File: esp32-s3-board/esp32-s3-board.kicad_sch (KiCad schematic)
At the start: 23 parts, among them J1 5077CR-16SMC2-BK-TR, Q1 UMH3N, U1 USBLC6-2P6, U2 LDL1117S33R, U3 CP2102N-Axx-xQFN28, U4 ESP32-S3-WROOM-1

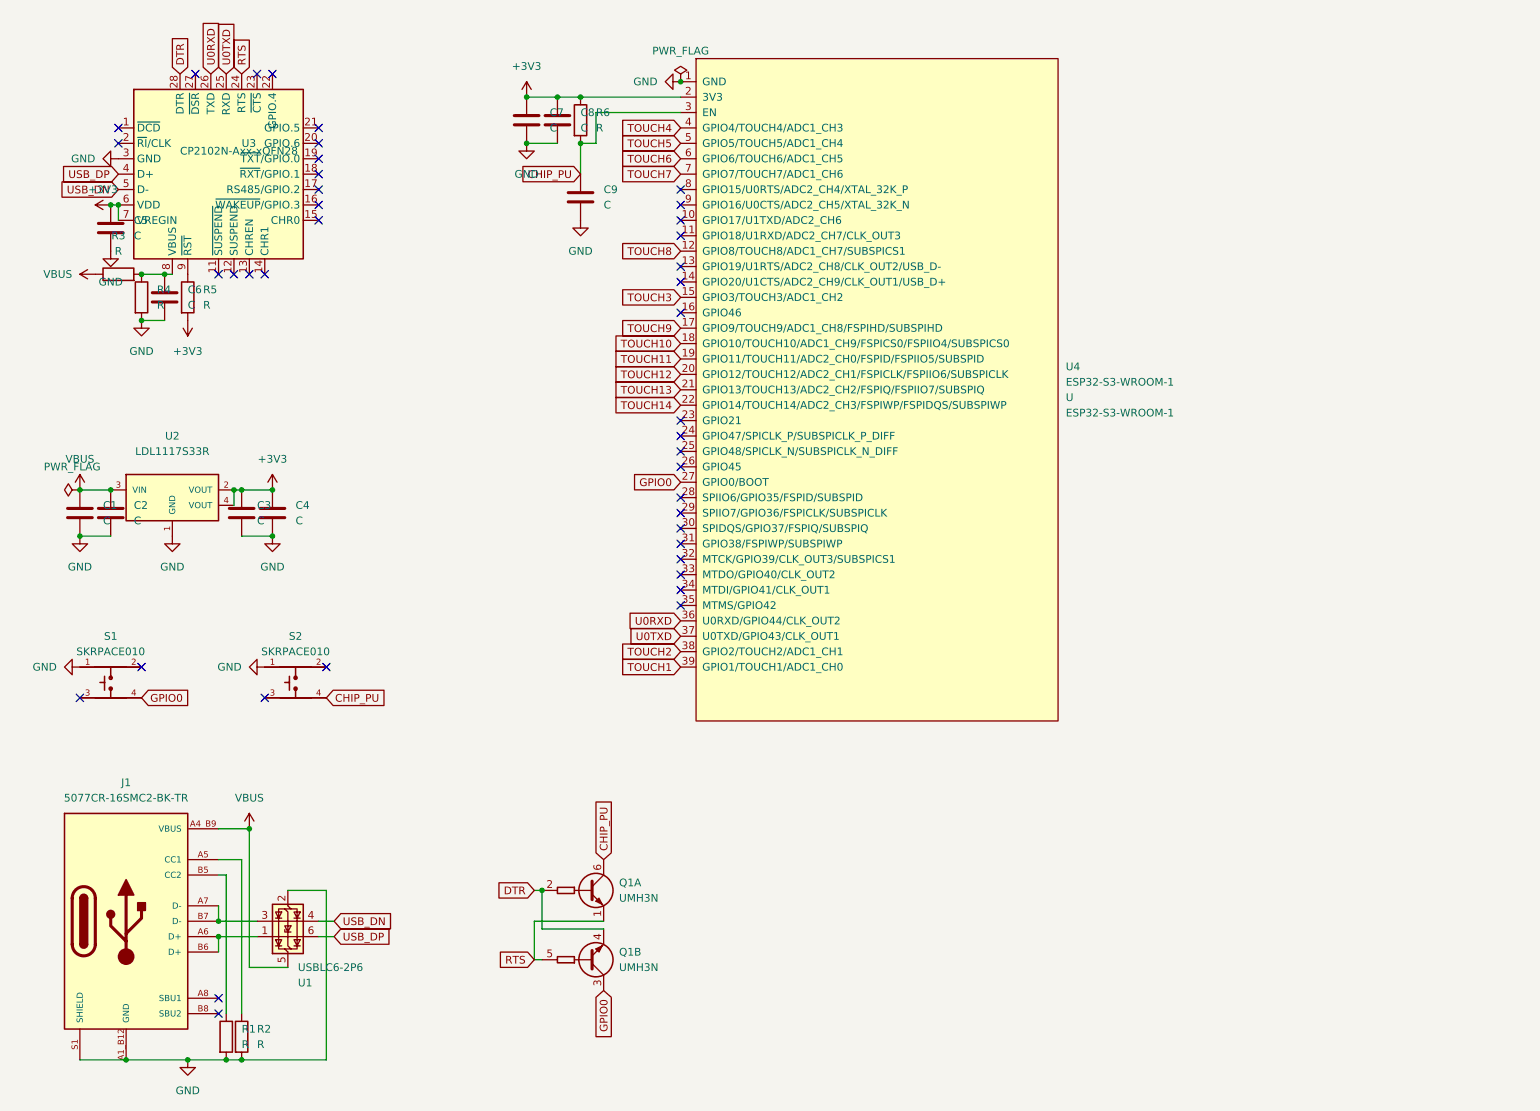
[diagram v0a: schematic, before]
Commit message: Add symbols and footprints libraries to esp32-s3-board
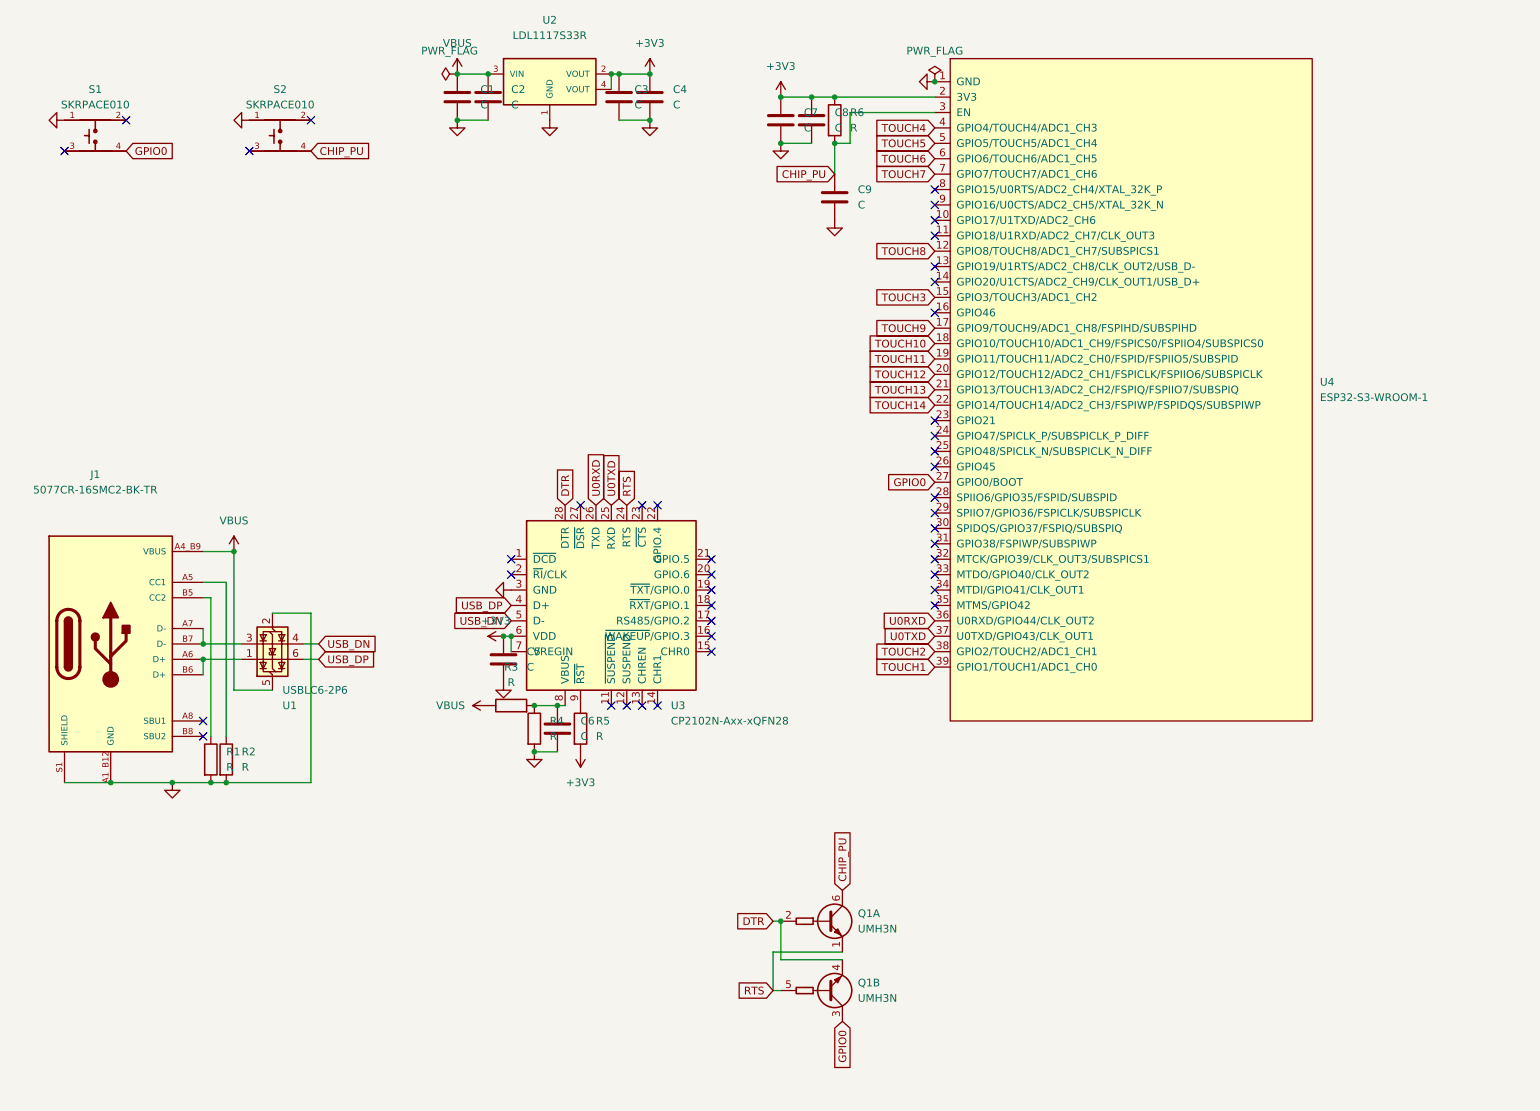
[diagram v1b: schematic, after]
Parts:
- removed U3: CP2102N-Axx-xQFN28, Package_DFN_QFN:QFN-28-1EP_5x5mm_P0.5mm_EP3.35x3.35mm, symbol Interface_USB:CP2102N-Axx-xQFN28
- removed U4: ESP32-S3-WROOM-1, RF_Module:ESP32-S3-WROOM-1, symbol Espressif:ESP32-S3-WROOM-1
- added U3: CP2102N-Axx-xQFN28, Package_DFN_QFN:QFN-28-1EP_5x5mm_P0.5mm_EP3.35x3.35mm, symbol CP2102N-Axx-xQFN28:CP2102N-Axx-xQFN28
- added U4: ESP32-S3-WROOM-1, RF_Module:ESP32-S3-WROOM-1, symbol ESP32-S3-WROOM-1:ESP32-S3-WROOM-1
- J1: footprint 5077CR-16SMC2-BK-TR:NELTRON_5077CR-16SMC2-BK-TR -> 5077CR-16SMC2-BK-TR:5077CR-16SMC2-BK-TR
- S1, S2: footprint SKRPACE010:SW_SKRPACE010 -> SKRPACE010:SKRPACE010
- U2: footprint LDL1117S33R:SOT230P700X180-4N -> LDL1117S33R:LDL1117S33R
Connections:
- net +3V3: now also U3.6 (VDD), U3.7 (VREGIN), U4.2 (3V3)
- net CHIP_PU: now also U4.3 (EN)
- net DTR: now also U3.28 (DTR)
- net GPIO0: now also U4.27 (GPIO0/BOOT)
- net RTS: now also U3.24 (RTS)
- net TOUCH1: now also U4.39 (GPIO1/TOUCH1/ADC1_CH0)
- net TOUCH10: now also U4.18 (GPIO10/TOUCH10/ADC1_CH9/FSPICS0/FSPIIO4/SUBSPICS0)
- net TOUCH11: now also U4.19 (GPIO11/TOUCH11/ADC2_CH0/FSPID/FSPIIO5/SUBSPID)
- net TOUCH12: now also U4.20 (GPIO12/TOUCH12/ADC2_CH1/FSPICLK/FSPIIO6/SUBSPICLK)
- net TOUCH13: now also U4.21 (GPIO13/TOUCH13/ADC2_CH2/FSPIQ/FSPIIO7/SUBSPIQ)
- net TOUCH14: now also U4.22 (GPIO14/TOUCH14/ADC2_CH3/FSPIWP/FSPIDQS/SUBSPIWP)
- net TOUCH2: now also U4.38 (GPIO2/TOUCH2/ADC1_CH1)
- net TOUCH3: now also U4.15 (GPIO3/TOUCH3/ADC1_CH2)
- net TOUCH4: now also U4.4 (GPIO4/TOUCH4/ADC1_CH3)
- net TOUCH5: now also U4.5 (GPIO5/TOUCH5/ADC1_CH4)
- net TOUCH6: now also U4.6 (GPIO6/TOUCH6/ADC1_CH5)
- net TOUCH7: now also U4.7 (GPIO7/TOUCH7/ADC1_CH6)
- net TOUCH8: now also U4.12 (GPIO8/TOUCH8/ADC1_CH7/SUBSPICS1)
- net TOUCH9: now also U4.17 (GPIO9/TOUCH9/ADC1_CH8/FSPIHD/SUBSPIHD)
- net U0RXD: now also U3.26 (TXD), U4.36 (U0RXD/GPIO44/CLK_OUT2)
- net U0TXD: now also U3.25 (RXD), U4.37 (U0TXD/GPIO43/CLK_OUT1)
- net USB_DN: now also U3.5 (D-)
- net USB_DP: now also U3.4 (D+)
- net at C6.2, R3.2, R4.1: now also U3.8 (VBUS)
- net at R5.1: now also U3.9 (~{RST})
- net GND renamed Earth
- net Earth: now also U3.29 (GND), U3.3 (GND), U4.1 (GND), U4.40 (GND), U4.41 (GND)

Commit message: Complete esp32-s3-board
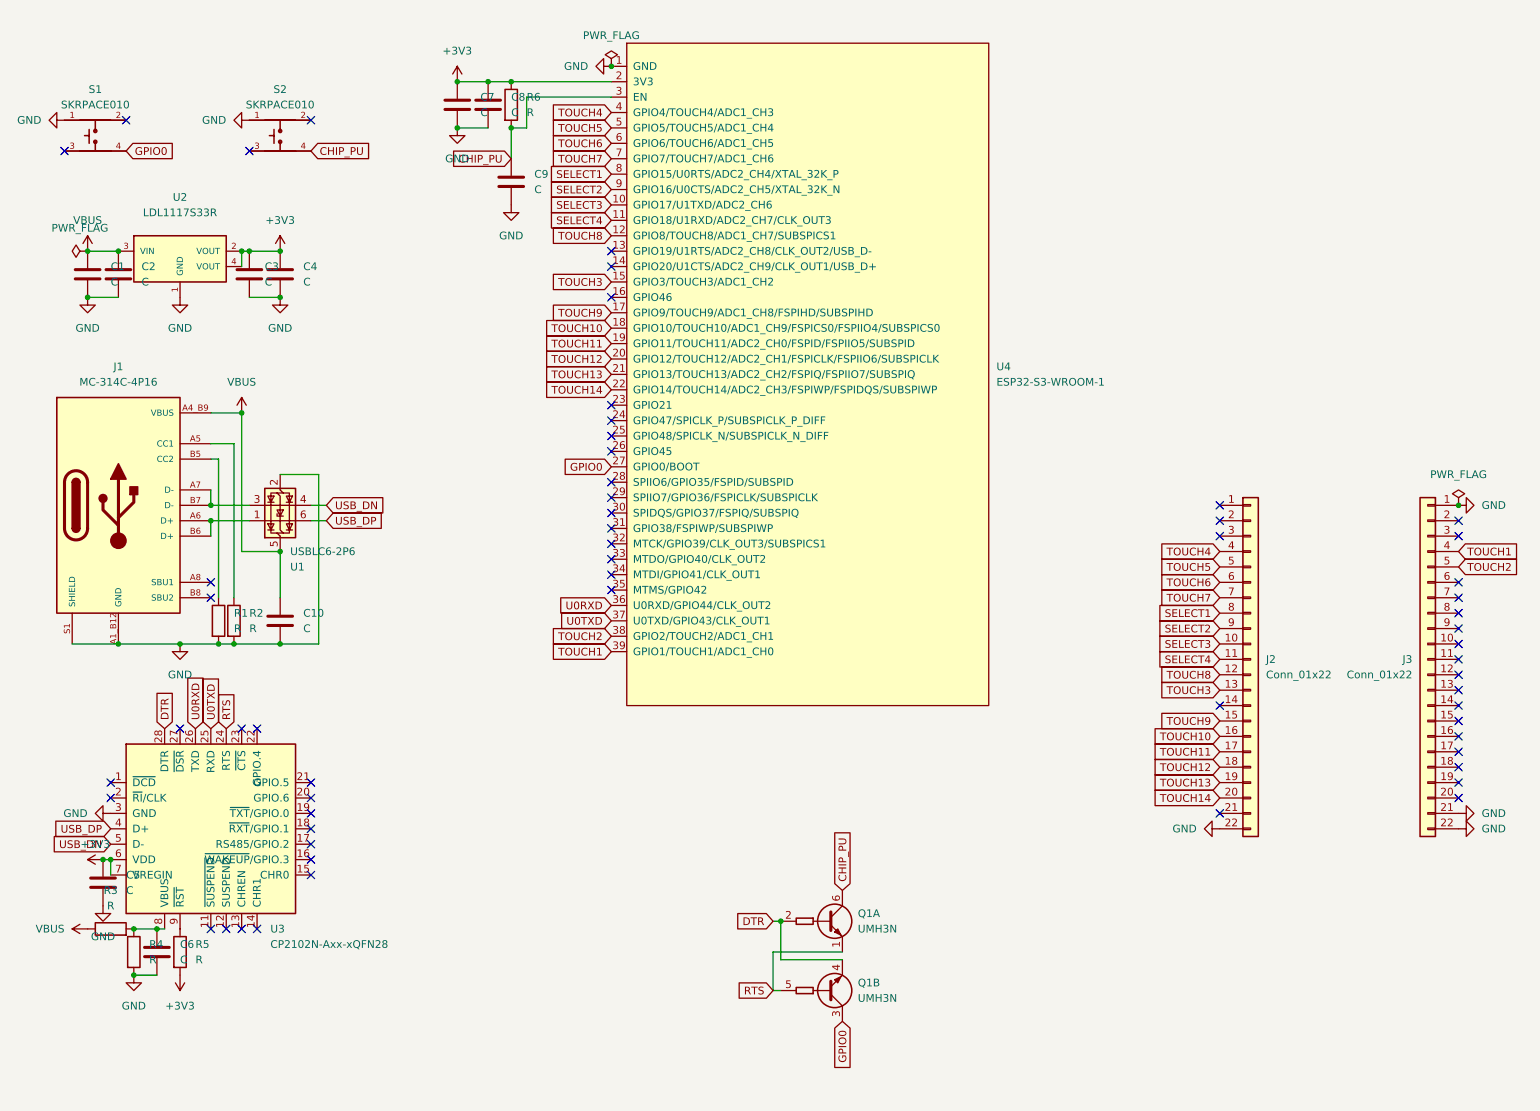
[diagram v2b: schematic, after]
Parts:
- added C10: C, Capacitor_SMD:C_0603_1608Metric_Pad1.08x0.95mm_HandSolder, symbol Device:C
- added J2, J3: Conn_01x22, Connector_PinHeader_2.54mm:PinHeader_1x22_P2.54mm_Vertical, symbol Connector_Generic:Conn_01x22
- J1: value 5077CR-16SMC2-BK-TR -> MC-314C-4P16; footprint 5077CR-16SMC2-BK-TR:5077CR-16SMC2-BK-TR -> MC-314C-4P16:USB-C-SMD_MC-314C-4P16
- U3: footprint Package_DFN_QFN:QFN-28-1EP_5x5mm_P0.5mm_EP3.35x3.35mm -> QFN-28-1EP_5x5mm_P0.5mm_EP3.35x3.35mm:QFN-28-1EP_5x5mm_P0.5mm_EP3.35x3.35mm
- U4: footprint RF_Module:ESP32-S3-WROOM-1 -> ESP32-S3-WROOM-1:ESP32-S3-WROOM-1
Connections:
- net TOUCH1: now also J3.4 (Pin_4)
- net TOUCH10: now also J2.16 (Pin_16)
- net TOUCH11: now also J2.17 (Pin_17)
- net TOUCH12: now also J2.18 (Pin_18)
- net TOUCH13: now also J2.19 (Pin_19)
- net TOUCH14: now also J2.20 (Pin_20)
- net TOUCH2: now also J3.5 (Pin_5)
- net TOUCH3: now also J2.13 (Pin_13)
- net TOUCH4: now also J2.4 (Pin_4)
- net TOUCH5: now also J2.5 (Pin_5)
- net TOUCH6: now also J2.6 (Pin_6)
- net TOUCH7: now also J2.7 (Pin_7)
- net TOUCH8: now also J2.12 (Pin_12)
- net TOUCH9: now also J2.15 (Pin_15)
- net VBUS: now also C10.2
- net SELECT3: now reaches U4.10 (GPIO17/U1TXD/ADC2_CH6)
- net SELECT3: now also J2.10 (Pin_10)
- net SELECT4: now reaches U4.11 (GPIO18/U1RXD/ADC2_CH7/CLK_OUT3)
- net SELECT4: now also J2.11 (Pin_11)
- net SELECT1: now reaches U4.8 (GPIO15/U0RTS/ADC2_CH4/XTAL_32K_P)
- net SELECT1: now also J2.8 (Pin_8)
- net SELECT2: now reaches U4.9 (GPIO16/U0CTS/ADC2_CH5/XTAL_32K_N)
- net SELECT2: now also J2.9 (Pin_9)
- net Earth renamed GND
- net GND: now also C10.1, J2.22 (Pin_22), J3.1 (Pin_1), J3.21 (Pin_21), J3.22 (Pin_22)
- no-connect marks 41 -> 59
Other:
- moved on the sheet: C1, C2, C3, C4, C5, C6, C7, C8, C9, J1, R1, R2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

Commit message: Add specific values to schematic
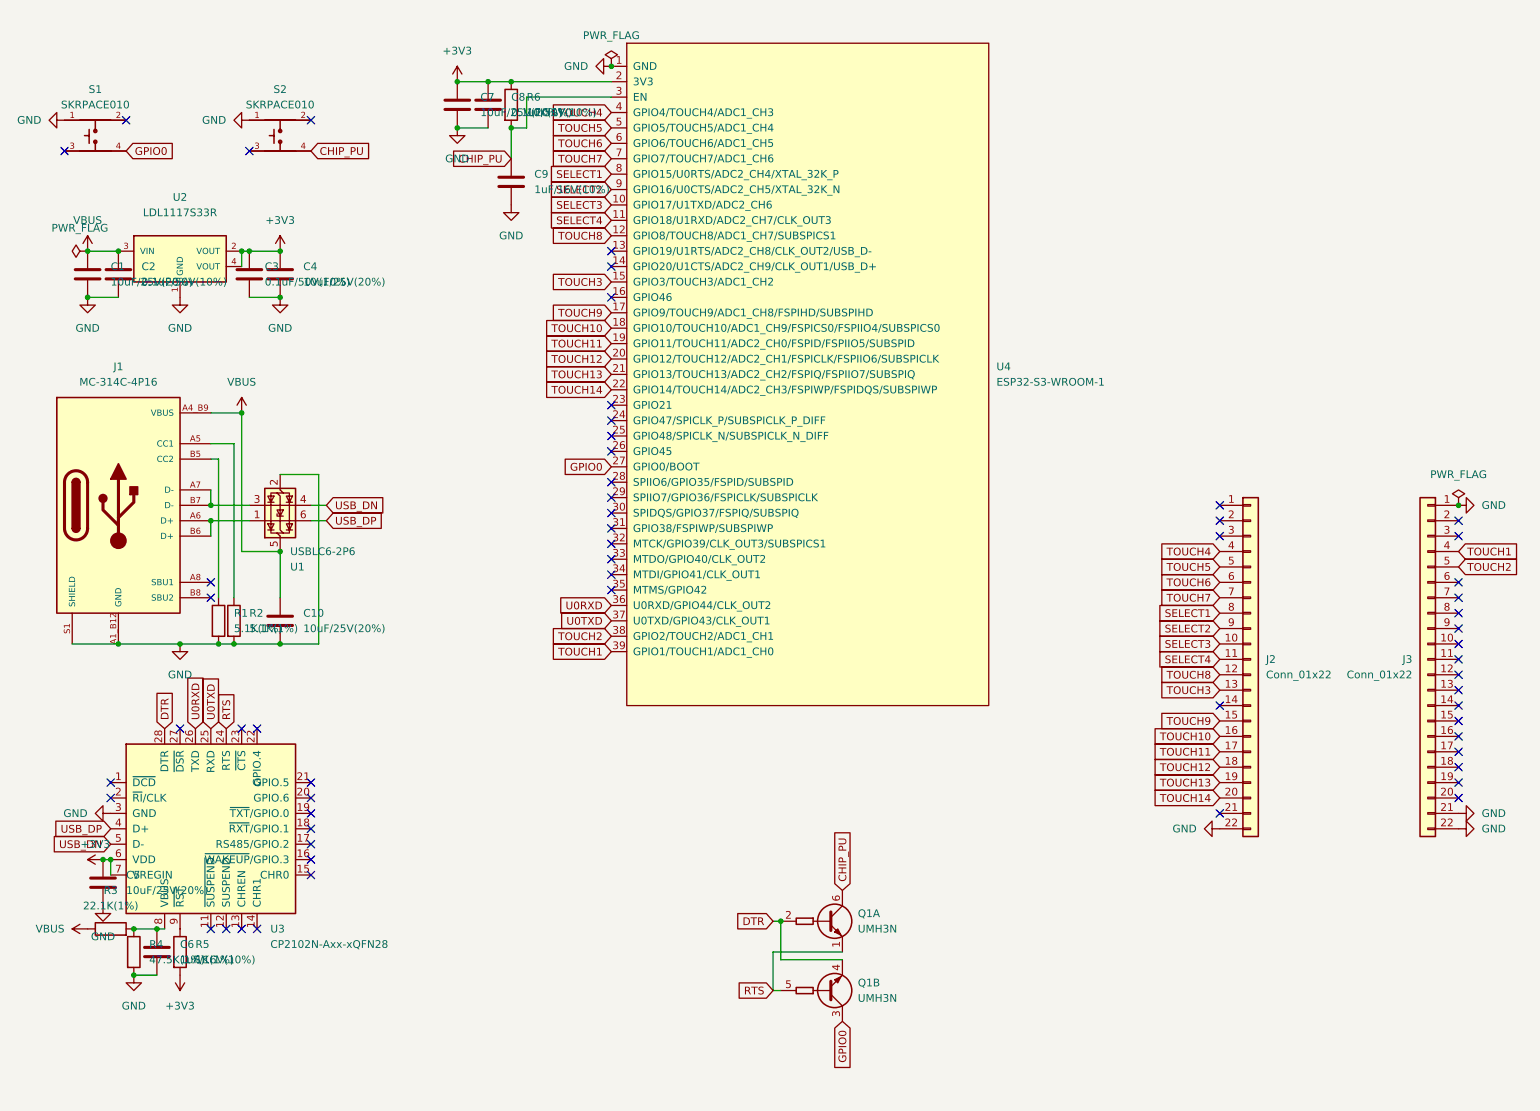
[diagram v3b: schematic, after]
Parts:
- C1, C10, C4, C5, C7: value C -> 10uF/25V(20%)
- C2, C3, C8: value C -> 0.1uF/50V(10%)
- C6, C9: value C -> 1uF/16V(10%)
- R1, R2: value R -> 5.1K(1%)
- R3: value R -> 22.1K(1%)
- R4: value R -> 47.5K(1%)
- R5: value R -> 1K(1%)
- R6: value R -> 10K(1%)
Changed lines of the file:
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@@
 			)
 		)
-		(property "Value" "C"
+		(property "Value" "0.1uF/50V(10%)"
 			(at 33.02 59.6899 0)
 			(effects
@@
 			)
 		)
-		(property "Value" "C"
+		(property "Value" "10uF/25V(20%)"
 			(at 59.69 116.8399 0)
 			(effects
@@
 			)
 		)
-		(property "Value" "C"
+		(property "Value" "0.1uF/50V(10%)"
 			(at 93.98 31.7499 0)
 			(effects
@@
 			)
 		)
-		(property "Value" "C"
+		(property "Value" "1uF/16V(10%)"
 			(at 39.37 171.4499 0)
 			(effects
@@
 			)
 		)
-		(property "Value" "R"
+		(property "Value" "22.1K(1%)"
 			(at 27.94 162.56 90)
 			(effects
@@
 			)
 		)
-		(property "Value" "R"
+		(property "Value" "10K(1%)"
 			(at 96.52 31.7499 0)
 			(effects
@@
 			)
 		)
-		(property "Value" "R"
+		(property "Value" "1K(1%)"
 			(at 41.91 171.4499 0)
 			(effects
@@
 			)
 		)
-		(property "Value" "R"
+		(property "Value" "5.1K(1%)"
 			(at 48.26 116.8399 0)
 			(effects
@@
 		(exclude_from_sim no)
 		(in_bom yes)
-		(on_board yes)
+		(on_board no)
 		(dnp no)
 		(fields_autoplaced yes)
@@
 			)
 		)
-		(property "Value" "R"
+		(property "Value" "5.1K(1%)"
 			(at 50.8 116.8399 0)
 			(effects
@@
 			)
 		)
-		(property "Value" "R"
+		(property "Value" "47.5K(1%)"
 			(at 34.29 171.4499 0)
 			(effects
@@
 			)
 		)
-		(property "Value" "C"
+		(property "Value" "1uF/16V(10%)"
 			(at 97.79 44.4499 0)
 			(effects
@@
 			)
 		)
-		(property "Value" "C"
+		(property "Value" "10uF/25V(20%)"
 			(at 27.94 59.6899 0)
 			(effects
@@
 			)
 		)
-		(property "Value" "C"
+		(property "Value" "10uF/25V(20%)"
 			(at 88.9 31.7499 0)
 			(effects
@@
 			)
 		)
-		(property "Value" "C"
+		(property "Value" "0.1uF/50V(10%)"
 			(at 53.34 59.6899 0)
 			(effects
@@
 			)
 		)
-		(property "Value" "C"
+		(property "Value" "10uF/25V(20%)"
 			(at 59.69 59.6899 0)
 			(effects
@@
 			)
 		)
-		(property "Value" "C"
+		(property "Value" "10uF/25V(20%)"
 			(at 30.48 160.0199 0)
 			(effects

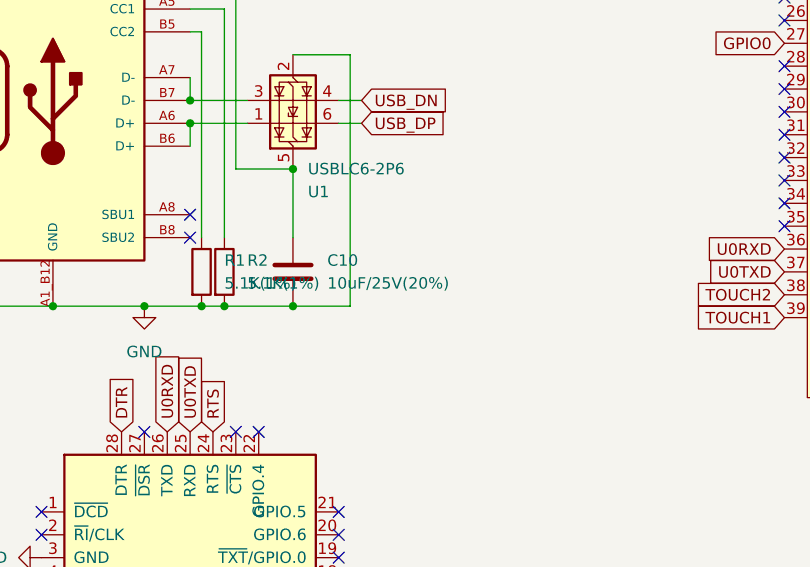
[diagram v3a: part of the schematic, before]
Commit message: Fix capacitor values
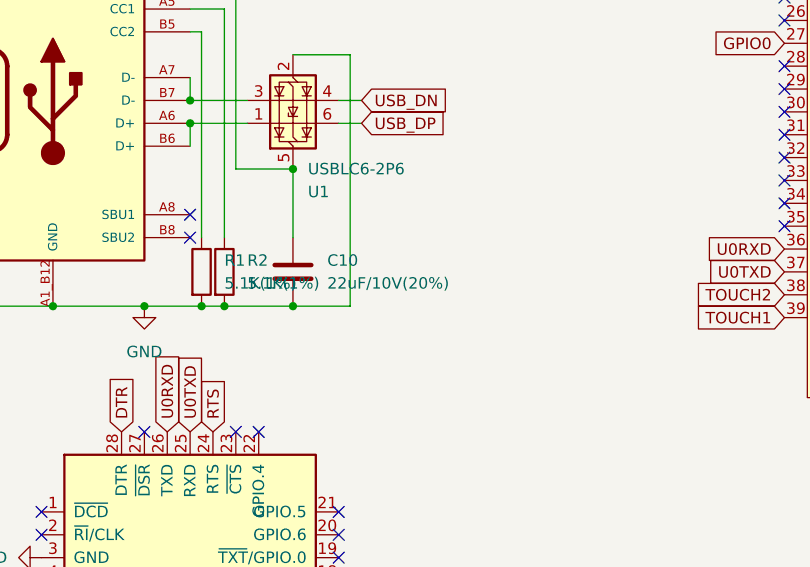
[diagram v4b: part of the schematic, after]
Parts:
- C10: value 10uF/25V(20%) -> 22uF/10V(20%)
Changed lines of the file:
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@@
 			)
 		)
-		(property "Value" "10uF/25V(20%)"
+		(property "Value" "22uF/10V(20%)"
 			(at 59.69 116.8399 0)
 			(effects
